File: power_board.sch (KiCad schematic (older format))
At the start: 32 parts, among them CON1 MICROUSB, J1 Conn_02x03_Odd_Even, J2 Conn_01x01, J3 Conn_01x01, J4 Conn_01x01, SW1 SW_Push, U1 PCA9555PW, U2 ATMEGA328P-AU, U3 PCA9555PW, U4 FT232RL, Y1 Crystal

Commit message: Removed PCA9555 and added PCA9685
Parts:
- removed U1, U3: PCA9555PW, Package_SO:TSSOP-24_4.4x7.8mm_P0.65mm, symbol Interface_Expansion:PCA9555PW
- added R46, R47: 10kR, lsts-passives:R_0603, symbol Device:R
- added U1, U3: PCA9685PW, Package_SO:TSSOP-28_4.4x9.7mm_P0.65mm, symbol Driver_LED:PCA9685PW
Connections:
- wire segments 199 -> 213
- no-connect marks 25 -> 23

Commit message: Replaced MCU by Arduino Nano
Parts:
- removed C10, C2, C5, C6, C8, C9: 100nF, lsts-passives:C_0603, symbol Device:C
- removed C3, C4: 22nF, lsts-passives:C_0603, symbol Device:C
- removed CON1: MICROUSB, lsts-conn:USB_Micro-B_Molex_47346-0001, symbol lsts-conn:MICROUSB
- removed D1, D2, D3: LED, LED_SMD:LED_0603_1608Metric, symbol Device:LED
- removed J1: Conn_02x03_Odd_Even, lsts-conn:CONN_ISP, symbol Connector_Generic:Conn_02x03_Odd_Even
- removed R3: 10kR, lsts-passives:R_0603, symbol Device:R
- removed R5, R6, R7: 1kR, lsts-passives:R_0603, symbol Device:R
- removed SW1: SW_Push, Button_Switch_SMD:SW_SPST_B3U-1000P, symbol Switch:SW_Push
- removed U2: ATMEGA328P-AU, lsts-ic:TQFP32, symbol lsts-micros:ATMEGA328P-AU
- removed U4: FT232RL, Package_SO:SSOP-28_5.3x10.2mm_P0.65mm, symbol Interface_USB:FT232RL
- removed Y1: Crystal, Crystal:Crystal_HC49-4H_Vertical, symbol Device:Crystal
- added A1: Arduino_Nano_v3.x, Module:Arduino_Nano, symbol MCU_Module:Arduino_Nano_v3.x
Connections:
- net labels removed: 5V_USB, AT_RXD, AT_TXD, D+, D-, LED, MISO, MOSI, RESET, SCK
- wire segments 213 -> 128
- no-connect marks 23 -> 3
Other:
- note added: "Address"

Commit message: Final touches
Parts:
- added R4, R7: 10kR, lsts_passives:R_0603, symbol Device:R
- C1: footprint lsts-passives:C_0603 -> lsts_passives:C_0603
- C2: renamed from C7; footprint lsts-passives:C_0603 -> lsts_passives:C_0603
- C3: renamed from C51; symbol Device:CP -> power_board-rescue:CP-Device
- J1: renamed from J2; footprint lsts-mecanical:MountingHole_3.5mm_Pad -> lsts_mecanical:MountingHole_3.5mm_Pad
- J2: renamed from J3; footprint lsts-mecanical:MountingHole_3.5mm_Pad -> lsts_mecanical:MountingHole_3.5mm_Pad
- J3: renamed from J4; footprint lsts-mecanical:MountingHole_3.5mm_Pad -> lsts_mecanical:MountingHole_3.5mm_Pad
- R1, R2: footprint lsts-passives:R_0603 -> lsts_passives:R_0603
- R3: renamed from R4; footprint lsts-passives:R_0603 -> lsts_passives:R_0603
- R5: renamed from R46; footprint lsts-passives:R_0603 -> lsts_passives:R_0603
- R6: renamed from R47; footprint lsts-passives:R_0603 -> lsts_passives:R_0603
- renumbered U3 to U2
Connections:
- net MTR7_EN is gone; now on net MTR6_SL: U2.16 (LED9)
- net MTR7_PH is gone; now on net MTR5_EN: U2.18 (LED11)
- net MTR7_SL is gone; now on net MTR6_PH: U2.17 (LED10)
- net MTR8_EN is gone; now on net PWM5_5V: U2.13 (LED7)
- net MTR8_PH is gone; now on net MTR6_EN: U2.15 (LED8)
- net MTR8_SL is gone; now on net PWM4_5V: U2.12 (LED6)
- net +5V_SB: now also R4.2, R7.2
- net GND: no longer U1.24 (A5), U2.24 (A5)
- net MTR1_EN: now also U1.20 (LED13); no longer U1.13 (LED7)
- net MTR1_PH: now also U1.22 (LED15); no longer U1.11 (LED5)
- net MTR1_SL: now also U1.21 (LED14); no longer U1.12 (LED6)
- net MTR2_EN: now also U1.17 (LED10); no longer U1.20 (LED13)
- net MTR2_PH: now also U1.19 (LED12); no longer U1.22 (LED15)
- net MTR2_SL: now also U1.18 (LED11); no longer U1.21 (LED14)
- net MTR3_EN: now also U1.13 (LED7); no longer U1.17 (LED10)
- net MTR3_PH: now also U1.11 (LED5); no longer U1.19 (LED12)
- net MTR3_SL: now also U1.12 (LED6); no longer U1.18 (LED11)
- net MTR5_EN: no longer U2.11 (LED5)
- net MTR5_PH: now also U2.20 (LED13); no longer U2.9 (LED3)
- net MTR5_SL: now also U2.19 (LED12); no longer U2.10 (LED4)
- net MTR6_EN: no longer U2.19 (LED12)
- net MTR6_PH: no longer U2.21 (LED14)
- net MTR6_SL: no longer U2.20 (LED13)
- net PWM1_5V: now also U2.9 (LED3); no longer A1.6 (D3)
- net PWM2_5V: now also U2.10 (LED4); no longer A1.8 (D5)
- net PWM3_5V: now also U2.11 (LED5); no longer A1.9 (D6)
- net PWM4_5V: no longer A1.12 (D9)
- net PWM5_5V: no longer A1.13 (D10)
- new net: R4.1, U1.24 (A5)
- new net: R7.1, U2.24 (A5)
- no-connect marks 3 -> 23

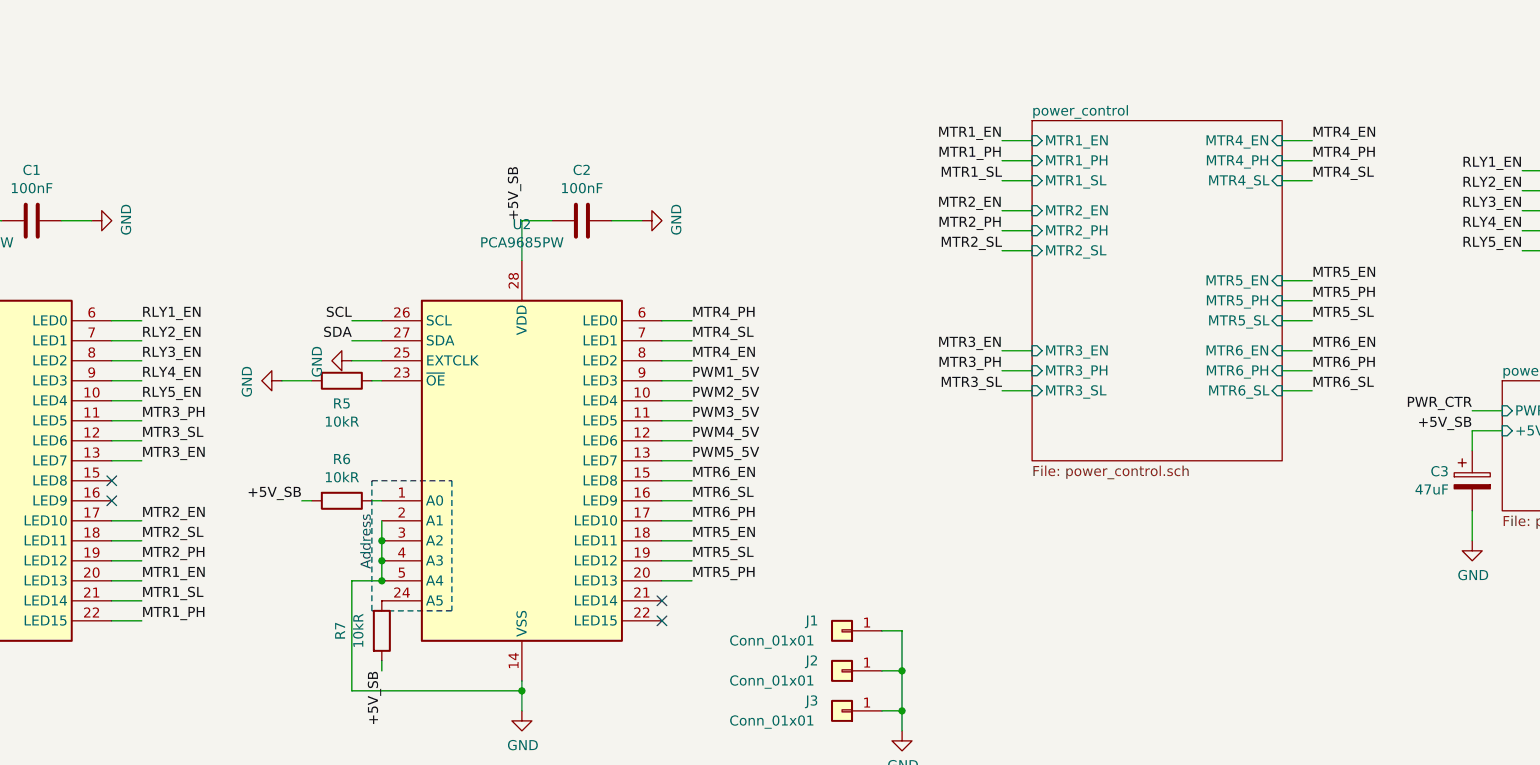
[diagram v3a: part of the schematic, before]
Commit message: Replaced motor drivers
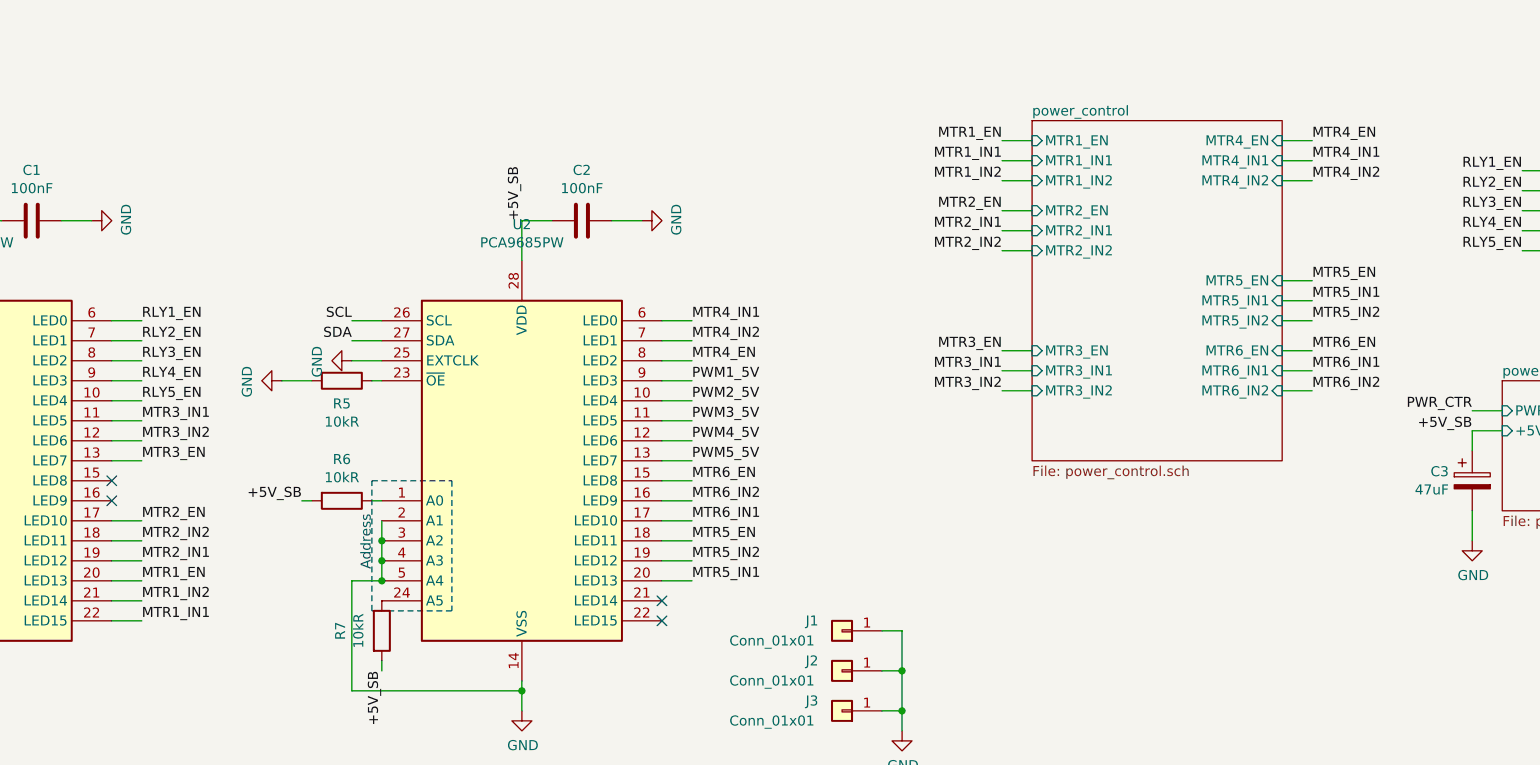
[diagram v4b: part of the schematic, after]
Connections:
- net MTR1_PH renamed MTR1_IN1
- net MTR1_SL renamed MTR1_IN2
- net MTR2_PH renamed MTR2_IN1
- net MTR2_SL renamed MTR2_IN2
- net MTR3_PH renamed MTR3_IN1
- net MTR3_SL renamed MTR3_IN2
- net MTR4_PH renamed MTR4_IN1
- net MTR4_SL renamed MTR4_IN2
- net MTR5_PH renamed MTR5_IN1
- net MTR5_SL renamed MTR5_IN2
- net MTR6_PH renamed MTR6_IN1
- net MTR6_SL renamed MTR6_IN2
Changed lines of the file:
@@
 MTR1_EN
 Text Label 7200 4650 2    50   ~ 0
-MTR1_PH
+MTR1_IN1
 Text Label 7200 4750 2    50   ~ 0
-MTR1_SL
+MTR1_IN2
 Text Label 7200 4900 2    50   ~ 0
 MTR2_EN
 Text Label 7200 5000 2    50   ~ 0
-MTR2_PH
+MTR2_IN1
 Text Label 7200 5100 2    50   ~ 0
-MTR2_SL
+MTR2_IN2
 Text Label 7200 5600 2    50   ~ 0
 MTR3_EN
 Text Label 7200 5700 2    50   ~ 0
-MTR3_PH
+MTR3_IN1
 Text Label 7200 5800 2    50   ~ 0
-MTR3_SL
+MTR3_IN2
 Text Label 8750 5250 0    50   ~ 0
 MTR5_EN
 Text Label 8750 5350 0    50   ~ 0
-MTR5_PH
+MTR5_IN1
 Text Label 8750 5450 0    50   ~ 0
-MTR5_SL
+MTR5_IN2
 Text Label 8750 5600 0    50   ~ 0
 MTR6_EN
 Text Label 8750 5700 0    50   ~ 0
-MTR6_PH
+MTR6_IN1
 Text Label 8750 5800 0    50   ~ 0
-MTR6_SL
+MTR6_IN2
 Text Label 8750 4750 0    50   ~ 0
-MTR4_SL
+MTR4_IN2
 Text Label 8750 4650 0    50   ~ 0
-MTR4_PH
+MTR4_IN1
 Text Label 8750 4550 0    50   ~ 0
 MTR4_EN
@@
 MTR1_EN
 Text Label 2900 6950 0    50   ~ 0
-MTR1_PH
+MTR1_IN1
 Text Label 2900 6850 0    50   ~ 0
-MTR1_SL
+MTR1_IN2
 Text Label 2900 6450 0    50   ~ 0
 MTR2_EN
 Text Label 2900 6650 0    50   ~ 0
-MTR2_PH
+MTR2_IN1
 Text Label 2900 6550 0    50   ~ 0
-MTR2_SL
+MTR2_IN2
 Text Label 5650 6550 0    50   ~ 0
 MTR5_EN
 Text Label 5650 6750 0    50   ~ 0
-MTR5_PH
+MTR5_IN1
 Text Label 5650 6650 0    50   ~ 0
-MTR5_SL
+MTR5_IN2
 Text Label 5650 6250 0    50   ~ 0
 MTR6_EN
 Text Label 5650 6450 0    50   ~ 0
-MTR6_PH
+MTR6_IN1
 Text Label 5650 6350 0    50   ~ 0
-MTR6_SL
+MTR6_IN2
 Text Label 5650 5550 0    50   ~ 0
-MTR4_SL
+MTR4_IN2
 Text Label 5650 5450 0    50   ~ 0
-MTR4_PH
+MTR4_IN1
 Text Label 5650 5650 0    50   ~ 0
 MTR4_EN
@@
 MTR3_EN
 Text Label 2900 5950 0    50   ~ 0
-MTR3_PH
+MTR3_IN1
 Text Label 2900 6050 0    50   ~ 0
-MTR3_SL
+MTR3_IN2
 $Comp
 L Driver_LED:PCA9685PW U2
@@
 F1 "power_control.sch" 50
 F2 "MTR1_EN" I L 7350 4550 50
-F3 "MTR1_PH" I L 7350 4650 50
-F4 "MTR1_SL" I L 7350 4750 50
+F3 "MTR1_IN1" I L 7350 4650 50
+F4 "MTR1_IN2" I L 7350 4750 50
 F5 "MTR2_EN" I L 7350 4900 50
-F6 "MTR2_PH" I L 7350 5000 50
-F7 "MTR2_SL" I L 7350 5100 50
+F6 "MTR2_IN1" I L 7350 5000 50
+F7 "MTR2_IN2" I L 7350 5100 50
 F8 "MTR3_EN" I L 7350 5600 50
-F9 "MTR3_PH" I L 7350 5700 50
-F10 "MTR3_SL" I L 7350 5800 50
+F9 "MTR3_IN1" I L 7350 5700 50
+F10 "MTR3_IN2" I L 7350 5800 50
 F11 "MTR4_EN" I R 8600 4550 50
-F12 "MTR4_PH" I R 8600 4650 50
-F13 "MTR4_SL" I R 8600 4750 50
+F12 "MTR4_IN1" I R 8600 4650 50
+F13 "MTR4_IN2" I R 8600 4750 50
 F14 "MTR5_EN" I R 8600 5250 50
-F15 "MTR5_PH" I R 8600 5350 50
-F16 "MTR5_SL" I R 8600 5450 50
+F15 "MTR5_IN1" I R 8600 5350 50
+F16 "MTR5_IN2" I R 8600 5450 50
 F17 "MTR6_EN" I R 8600 5600 50
-F18 "MTR6_PH" I R 8600 5700 50
-F19 "MTR6_SL" I R 8600 5800 50
+F18 "MTR6_IN1" I R 8600 5700 50
+F19 "MTR6_IN2" I R 8600 5800 50
 $EndSheet
 Text Label 2900 5850 0    50   ~ 0

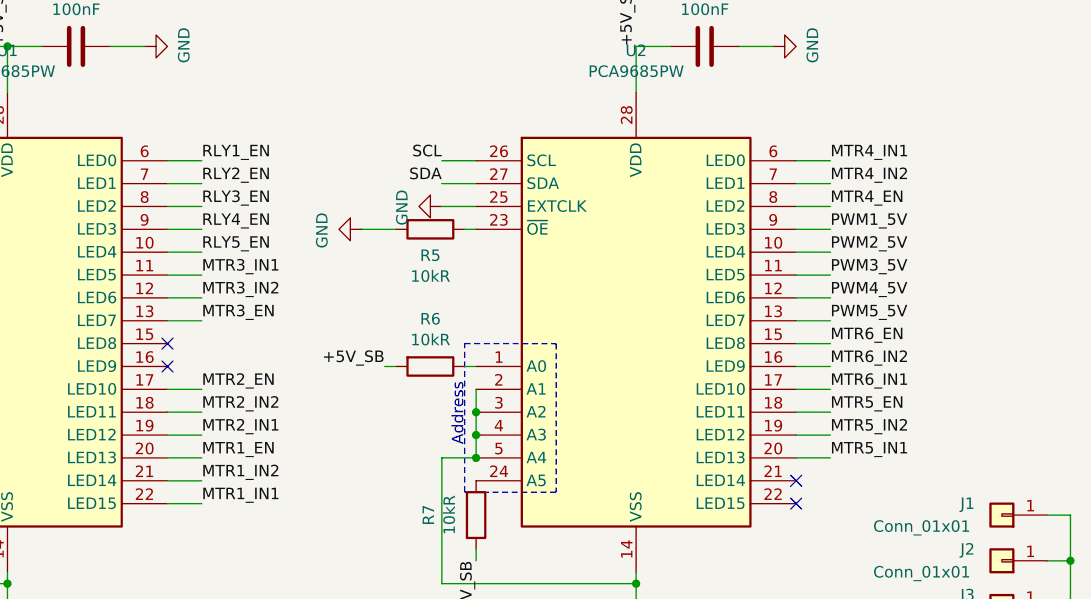
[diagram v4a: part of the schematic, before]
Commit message: Replaced driver footprints
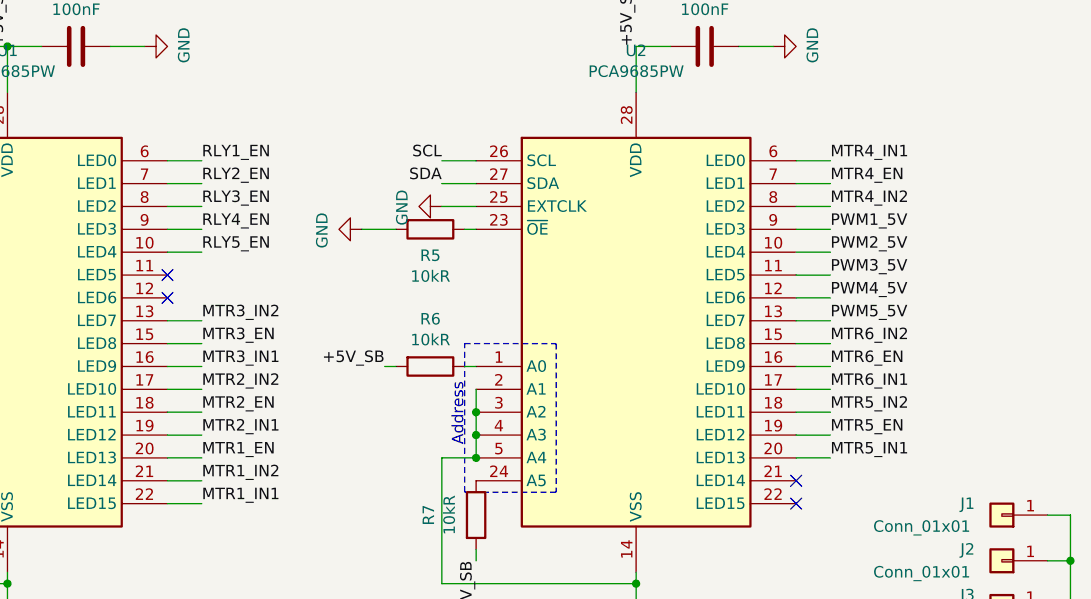
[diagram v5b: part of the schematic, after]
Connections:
- net MTR2_EN: now also U1.18 (LED11); no longer U1.17 (LED10)
- net MTR2_IN2: now also U1.17 (LED10); no longer U1.18 (LED11)
- net MTR3_EN: now also U1.15 (LED8); no longer U1.13 (LED7)
- net MTR3_IN1: now also U1.16 (LED9); no longer U1.11 (LED5)
- net MTR3_IN2: now also U1.13 (LED7); no longer U1.12 (LED6)
- net MTR4_EN: now also U2.7 (LED1); no longer U2.8 (LED2)
- net MTR4_IN2: now also U2.8 (LED2); no longer U2.7 (LED1)
- net MTR5_EN: now also U2.19 (LED12); no longer U2.18 (LED11)
- net MTR5_IN2: now also U2.18 (LED11); no longer U2.19 (LED12)
- net MTR6_EN: now also U2.16 (LED9); no longer U2.15 (LED8)
- net MTR6_IN2: now also U2.15 (LED8); no longer U2.16 (LED9)
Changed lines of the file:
@@
 	2750 6150 2900 6150
 Wire Wire Line
-	2750 5950 2900 5950
-Wire Wire Line
-	2750 6050 2900 6050
-Wire Wire Line
 	2750 6750 2900 6750
 Wire Wire Line
 	2750 6850 2900 6850
-Wire Wire Line
-	2750 6450 2900 6450
 Wire Wire Line
 	2750 6650 2900 6650
@@
 	0    -1   -1   0
 $EndComp
-NoConn ~ 2750 6250
-NoConn ~ 2750 6350
 Wire Wire Line
 	2750 6950 2900 6950
@@
 Text Label 2900 6850 0    50   ~ 0
 MTR1_IN2
-Text Label 2900 6450 0    50   ~ 0
+Text Label 2900 6550 0    50   ~ 0
 MTR2_EN
 Text Label 2900 6650 0    50   ~ 0
 MTR2_IN1
-Text Label 2900 6550 0    50   ~ 0
-MTR2_IN2
-Text Label 5650 6550 0    50   ~ 0
+Text Label 5650 6650 0    50   ~ 0
 MTR5_EN
 Text Label 5650 6750 0    50   ~ 0
 MTR5_IN1
-Text Label 5650 6650 0    50   ~ 0
+Text Label 5650 6550 0    50   ~ 0
 MTR5_IN2
-Text Label 5650 6250 0    50   ~ 0
+Text Label 5650 6350 0    50   ~ 0
 MTR6_EN
 Text Label 5650 6450 0    50   ~ 0
 MTR6_IN1
-Text Label 5650 6350 0    50   ~ 0
+Text Label 5650 6250 0    50   ~ 0
 MTR6_IN2
-Text Label 5650 5550 0    50   ~ 0
+Text Label 5650 5650 0    50   ~ 0
 MTR4_IN2
 Text Label 5650 5450 0    50   ~ 0
 MTR4_IN1
-Text Label 5650 5650 0    50   ~ 0
+Text Label 5650 5550 0    50   ~ 0
 MTR4_EN
+Text Label 2900 6250 0    50   ~ 0
+MTR3_EN
+Text Label 2900 6350 0    50   ~ 0
+MTR3_IN1
 Text Label 2900 6150 0    50   ~ 0
-MTR3_EN
-Text Label 2900 5950 0    50   ~ 0
-MTR3_IN1
-Text Label 2900 6050 0    50   ~ 0
 MTR3_IN2
 $Comp
@@
 	1    0    0    -1
 $EndComp
-$Comp
-L Driver_LED:PCA9685PW U1
-U 1 1 5E7BE61E
-P 2050 6150
-F 0 "U1" H 2050 7331 50  0000 C CNN
-F 1 "PCA9685PW" H 2050 7240 50  0000 C CNN
-F 2 "Package_SO:TSSOP-28_4.4x9.7mm_P0.65mm" H 2075 5175 50  0001 L CNN
-F 3 "http://www.nxp.com/documents/data_sheet/PCA9685.pdf" H 1650 6850 50  0001 C CNN
-	1    2050 6150
-	1    0    0    -1
-$EndComp
 Wire Wire Line
 	1050 4950 1050 5050
@@
 Wire Wire Line
 	1250 4950 2050 4950
-Wire Wire Line
-	1350 6350 1350 6450
-Connection ~ 1350 6450
-Wire Wire Line
-	1350 6450 1350 6550
-Connection ~ 1350 6550
-Wire Wire Line
-	1350 6550 1350 6650
-Connection ~ 1350 6650
-Wire Wire Line
-	1350 6650 1350 6750
 Wire Wire Line
 	1350 5650 1200 5650
@@
 Wire Wire Line
 	2050 7300 2050 7400
+Wire Wire Line
+	3950 7300 3950 6750
+Wire Wire Line
+	3950 6750 4100 6750
+Wire Wire Line
+	3950 7300 4800 7300
+Wire Wire Line
+	2750 6350 2900 6350
 Connection ~ 1350 6750
 Wire Wire Line
-	3950 7300 3950 6750
-Wire Wire Line
-	3950 6750 4100 6750
-Wire Wire Line
-	3950 7300 4800 7300
+	1350 6650 1350 6750
+Connection ~ 1350 6650
+Wire Wire Line
+	1350 6550 1350 6650
+Connection ~ 1350 6550
+Wire Wire Line
+	1350 6350 1350 6450
+Wire Wire Line
+	1350 6450 1350 6550
+Connection ~ 1350 6450
+$Comp
+L Driver_LED:PCA9685PW U1
+U 1 1 5E7BE61E
+P 2050 6150
+F 0 "U1" H 2050 7331 50  0000 C CNN
+F 1 "PCA9685PW" H 2050 7240 50  0000 C CNN
+F 2 "Package_SO:TSSOP-28_4.4x9.7mm_P0.65mm" H 2075 5175 50  0001 L CNN
+F 3 "http://www.nxp.com/documents/data_sheet/PCA9685.pdf" H 1650 6850 50  0001 C CNN
+	1    2050 6150
+	1    0    0    -1
+$EndComp
+Wire Wire Line
+	2750 6250 2900 6250
+Wire Wire Line
+	2750 6450 2900 6450
+Text Label 2900 6450 0    50   ~ 0
+MTR2_IN2
+NoConn ~ 2750 5950
+NoConn ~ 2750 6050
 $EndSCHEMATC
